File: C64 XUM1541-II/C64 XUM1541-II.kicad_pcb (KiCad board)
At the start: 2 copper layers, 64.1 x 39.4 mm, 18 parts, among them J1 C64_IEC, J2 SpeedDOS, M1 Mounting, M2 Mounting, M3 Mounting, M4 Mounting, SW1 RESET, U1 7406

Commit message: First new layout draft
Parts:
- added D2: ACTIVITY, LED_THT:LED_D5.0mm, F.Cu at (104.8, 94.0)
- added REF***: KiCad-Logo2_6mm_SilkScreen, Symbols:KiCad-Logo2_6mm_SilkScreen, B.Cu at (191.3, 126.9)
- D1: footprint LEDs:LED_D5.0mm -> LED_THT:LED_D5.0mm
- R4: value 100k -> 330
- moved M1 83.4 mm to (102.9, 100.3)
- moved R4 66.6 mm to (111.1, 83.8), turned to 270 degrees
- moved M4 65.4 mm to (102.9, 57.8)
- moved J2 48.0 mm to (135.3, 61.0)
- moved R2 46.2 mm to (156.8, 91.4), turned to 270 degrees
- moved M2 45.7 mm to (167.0, 100.3)
- moved R6 43.8 mm to (153.0, 91.4), turned to 270 degrees
- moved R3 42.5 mm to (145.4, 91.4), turned to 270 degrees
- moved U1 42.3 mm to (145.4, 87.6), turned to 90 degrees
- moved J1 41.9 mm to (153.0, 67.3)
- moved R5 38.8 mm to (160.7, 91.4), turned to 270 degrees
- moved R7 34.0 mm to (149.2, 91.4), turned to 270 degrees
- moved SW1 31.6 mm to (104.8, 73.7), turned to 90 degrees
- moved C1 22.3 mm to (141.6, 81.3), turned to 270 degrees
- moved R1 22.3 mm to (111.1, 81.3), turned to 90 degrees
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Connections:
- R4 pad 1: Net-(R4-Pad1) -> VCC
- R4 pad 2: GND -> Net-(D2-Pad2)
- U1 pad 1: Net-(R4-Pad1) -> /CLK
- U1 pad 2: (no net) -> ACT
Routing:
- net /RESET: track 0.00 -> 75.3 mm, vias 0 -> 2
- net /CLK_IN: track 0.00 -> 73.9 mm, vias 0 -> 2
- net /DATA: track 0.00 -> 72.0 mm, vias 0 -> 2
- net /D4: track 64.7 -> 0.00 mm, vias 2 -> 0
- net /ATN_IN: track 2.54 -> 65.9 mm
- net /D5: track 58.3 -> 0.00 mm, vias 2 -> 0
- net /CLK: track 0.00 -> 56.5 mm, vias 0 -> 1
- net ACT: track 0.00 -> 54.9 mm
- net /DATA_IN: track 2.54 -> 52.2 mm, vias 0 -> 1
- net /D2: track 49.4 -> 0.00 mm
- net /D6: track 47.3 -> 0.00 mm, vias 2 -> 0
- net /D3: track 47.3 -> 0.00 mm
- net /ATN: track 0.00 -> 47.0 mm, vias 0 -> 1
- net /DATA3: track 0.00 -> 46.5 mm, vias 0 -> 1
- net /D1: track 44.3 -> 0.00 mm
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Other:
- board size 64.1 x 39.4 mm -> 70.5 x 48.9 mm
- net class Power: clearance 0.2 -> 0.381; trace_width 1 -> 0.381; via_dia 1 -> 0.6; via_drill 0.6 -> 0.4
- rule pad_to_mask_clearance: 0.2 -> 0
- board text added: "PI1541-II Module (rev. C) github.com/tebl Licensed under CERN OHL v.1.2"
- board text removed: "C64 XUM1541"
- board text removed: "Revision B"
- board text removed: "github.com/tebl"

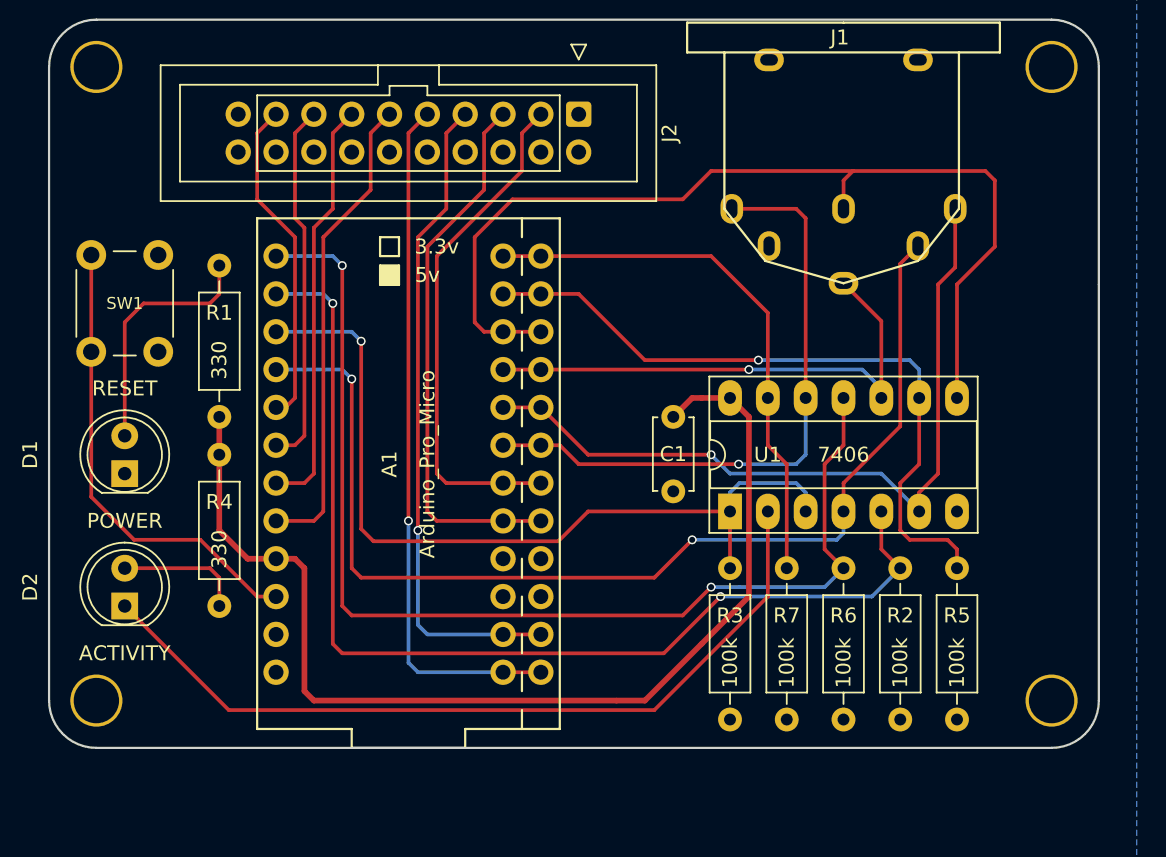
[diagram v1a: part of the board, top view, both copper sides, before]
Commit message: Silkscreen tweaks and gerber exports
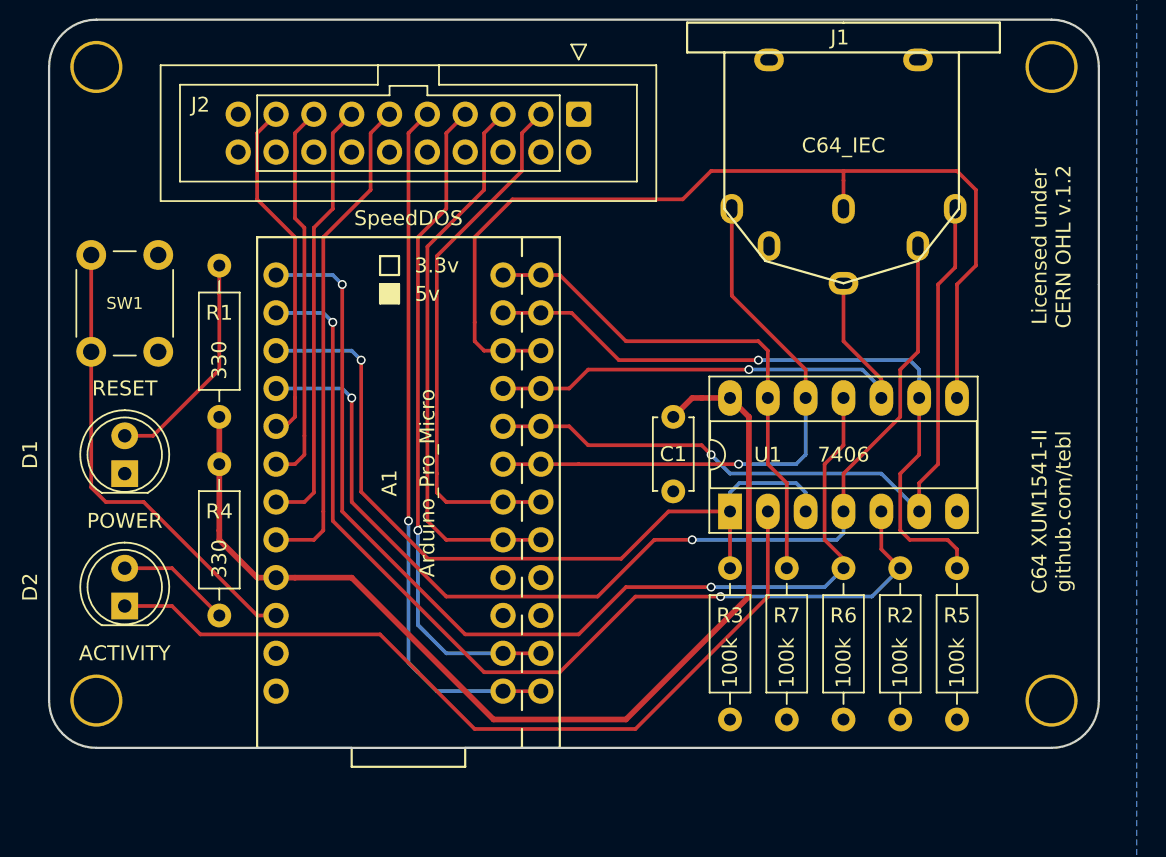
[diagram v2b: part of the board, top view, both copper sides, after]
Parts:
- moved REF*** 48.9 mm to (153.0, 96.5)
- moved A1 1.27 mm to (123.8, 85.7)
- moved R4 0.64 mm to (111.1, 84.5)
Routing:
- net /DATA: track 72.0 -> 66.9 mm
- net /RESET: track 75.3 -> 71.3 mm
- net /SRQ_IN: track 42.2 -> 39.1 mm
- net /CLK_IN: track 73.9 -> 71.1 mm
- net VCC: track 73.8 -> 71.1 mm
- net /SRQ: track 37.0 -> 35.0 mm
- net /CLK: track 56.5 -> 54.7 mm
- net Net-(D1-Pad2): track 16.7 -> 15.2 mm
- net /DATA2: track 44.1 -> 45.5 mm
- net /DATA3: track 46.5 -> 47.9 mm
- net /DATA0: track 34.3 -> 35.5 mm
- net /DATA7: track 22.2 -> 23.4 mm
- net /DATA5: track 28.0 -> 29.3 mm
- net /DATA4: track 31.9 -> 33.2 mm
- net /DATA6: track 24.5 -> 25.8 mm
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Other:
- board text added: "(read documentation before use)"
- board text added: "C64 XUM1541-II github.com/tebl"
- board text added: "Licensed under CERN OHL v.1.2"
- board text removed: "PI1541-II Module (rev. C) github.com/tebl Licensed under CERN OHL v.1.2"

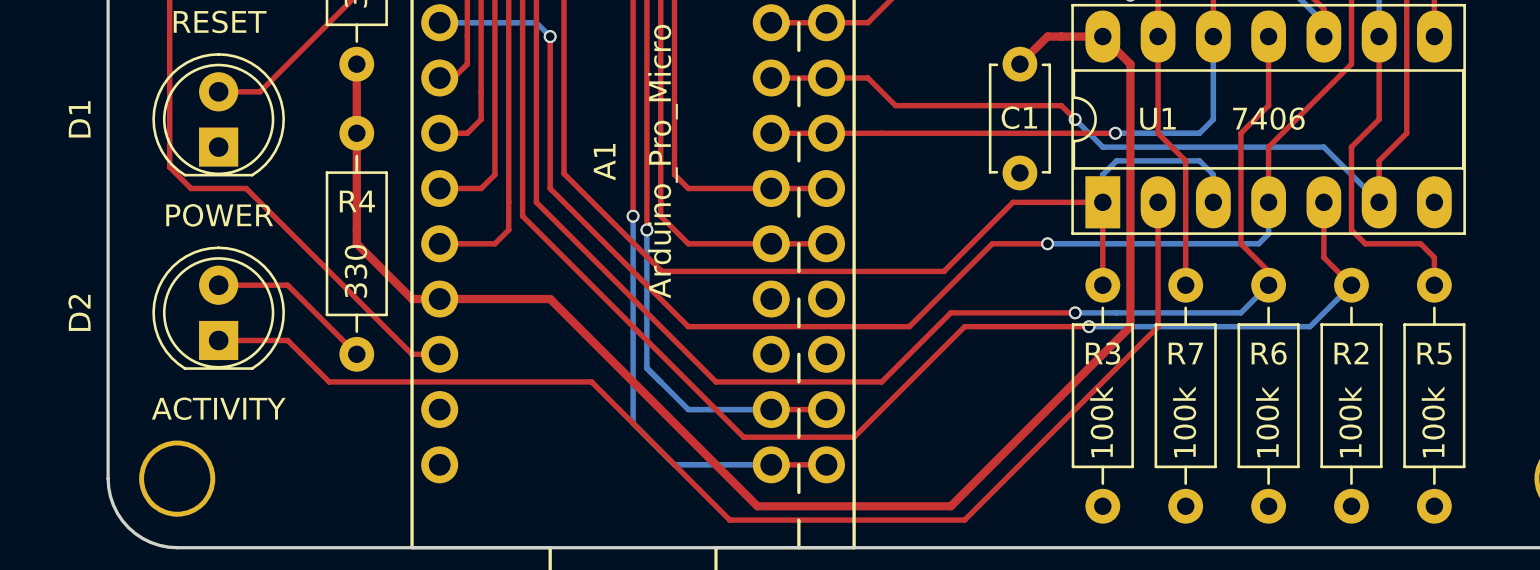
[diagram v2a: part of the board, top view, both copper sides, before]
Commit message: ACTIVITY is now DRIVE LED
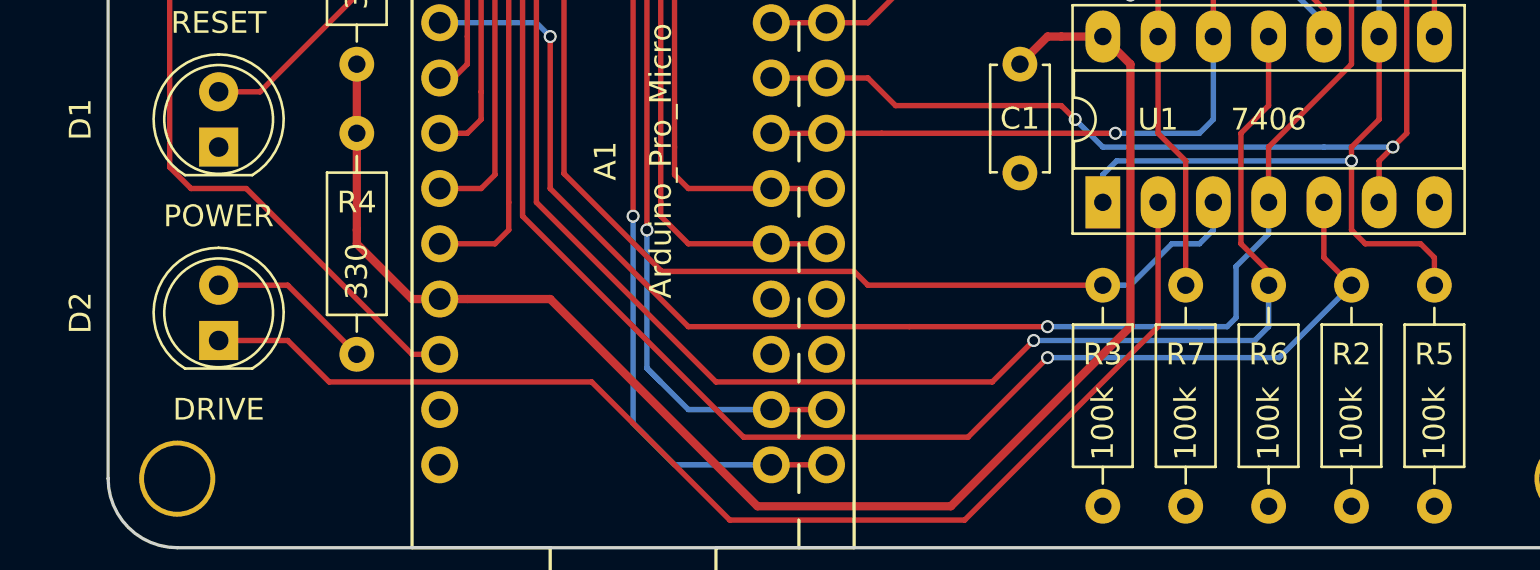
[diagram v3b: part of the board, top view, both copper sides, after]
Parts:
- D2: value ACTIVITY -> DRIVE
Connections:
- U1 pad 1: /CLK -> /ATN
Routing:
- net /ATN: track 46.4 -> 59.4 mm, vias 1 -> 2
- net /CLK: track 54.7 -> 49.1 mm
- net /CLK_IN: track 71.1 -> 72.5 mm
- net /RESET: track 71.3 -> 72.5 mm
- net /DATA_IN: track 51.6 -> 51.2 mm, vias 1 -> 2

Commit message: Updated silkscreen
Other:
- board text added: "C64 XUM1541-II Board revison B github.com/tebl"

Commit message: Moved connector to clear stepper motor
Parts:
- moved J2 23.0 mm to (112.4, 63.5), turned to 90 degrees
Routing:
- net /DATA3: track 47.9 -> 2.54 mm, vias 1 -> 0
- net /DATA2: track 45.5 -> 2.54 mm, vias 1 -> 0
- net /DATA1: track 37.6 -> 2.54 mm
- net /DATA0: track 35.5 -> 2.54 mm
- net /DATA7: track 23.4 -> 35.1 mm, vias 0 -> 1
- net /DATA6: track 25.8 -> 35.1 mm, vias 0 -> 1
- net /DATA5: track 29.3 -> 35.1 mm, vias 0 -> 1
- net /DATA4: track 33.2 -> 35.1 mm
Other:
- rule trace_min: 0.2 -> 0

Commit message: Rotated parallel connector
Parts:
- R1, R4: value 330 -> 470
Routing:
- net /DATA3: track 2.54 -> 43.8 mm, vias 0 -> 2
- net /DATA2: track 2.54 -> 42.3 mm, vias 0 -> 2
- net /DATA0: track 2.54 -> 39.4 mm, vias 0 -> 2
- net /DATA1: track 2.54 -> 36.4 mm, vias 0 -> 2
- net /ATN_IN: track 64.4 -> 62.7 mm

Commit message: Updated gerber files and small tweaks
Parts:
- J1: value C64_IEC -> IEC
- J2: value SpeedDOS -> PARALLEL
